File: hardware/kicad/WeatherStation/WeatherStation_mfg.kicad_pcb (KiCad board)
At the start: 4 copper layers, 100 x 80 mm, 120 parts, among them J1 USB-C, J10 SOIL_TEMP, J11 LEAF_WET, J12 PYRANOMETER, J13 PANEL_TEMP_F, J14 PANEL_TEMP_B, J15 POWER_PULSE, J16 RS485_Bus, J18 SMA_WiFi, J19 RJ45_Magjack, J2 SOLAR_IN, J20 NanoSIM, J21 SMA_LTE, J22 MicroSD, J3 BATTERY, J4 ANEMOMETER, J5 RAIN_GAUGE, J6 SMA_LoRa, J7 DEBUG_UART, J8 SOIL_MOIST_1, J9 SOIL_MOIST_2, SW1 BOOT, SW2 RESET, SW3 MODE_DIP, U10 STM32F407VGT6, U11 MAX3485ESA+, U12 ATWINC1500, U13 RN4870-I/RM, U14 W5500, U15 SIM7600E-H, U16 TPS7A2033, U2 TP4056, U3 AMS1117-3.3, U4 BME280, U5 AS5600, U6 SI1145, U7 BH1750FVI, U8 SX1276/RFM95W, Y1 8MHz, Y2 25MHz

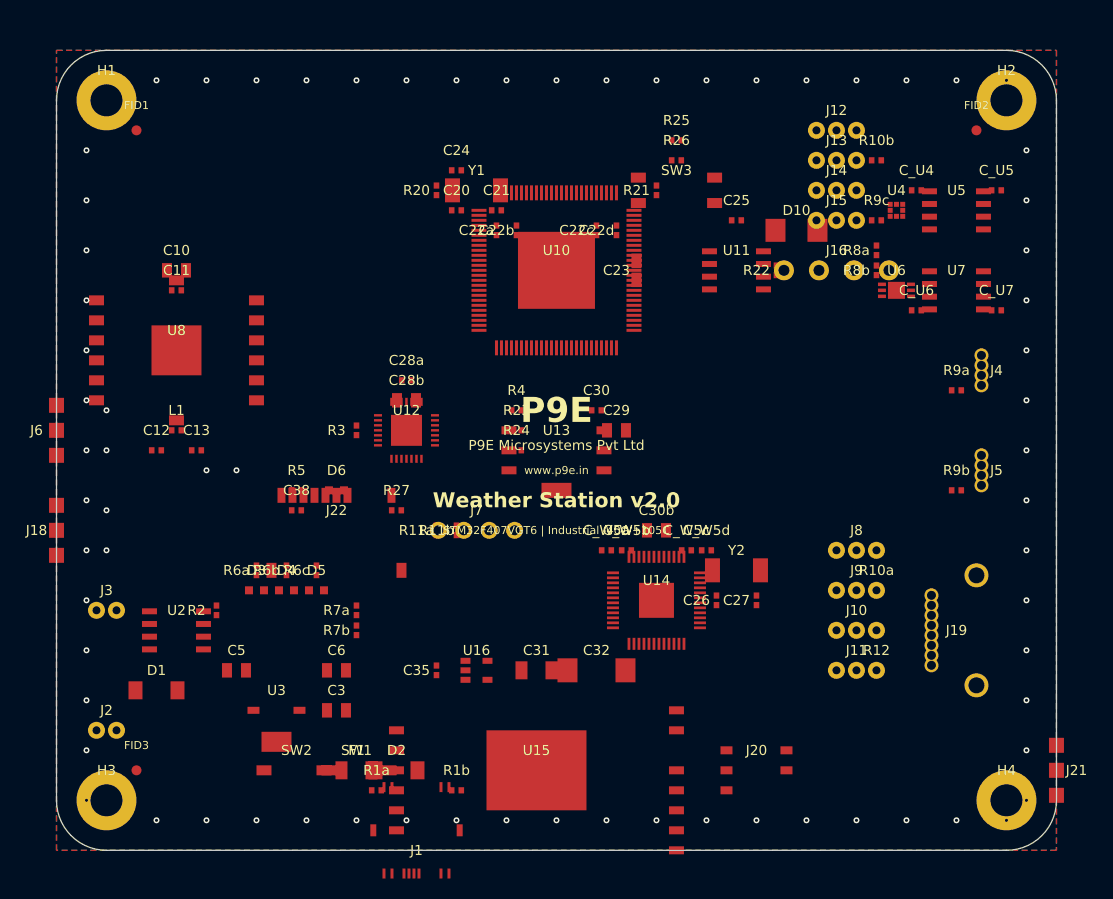
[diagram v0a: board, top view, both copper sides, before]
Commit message: fix: add 3 missing BOM components to manufacturing PCB
Add U2A (DW01A battery protection IC), Q1 (FS8205A dual N-MOSFET
for battery protection), and C4 (1uF AS5600 decoupling cap) that
were missing from the PCB layout. All BOM components now have
corresponding footprints in the manufacturing PCB.

https://claude.ai/code/session_01XHnfZQ5BbxTCTBMCteQyVe
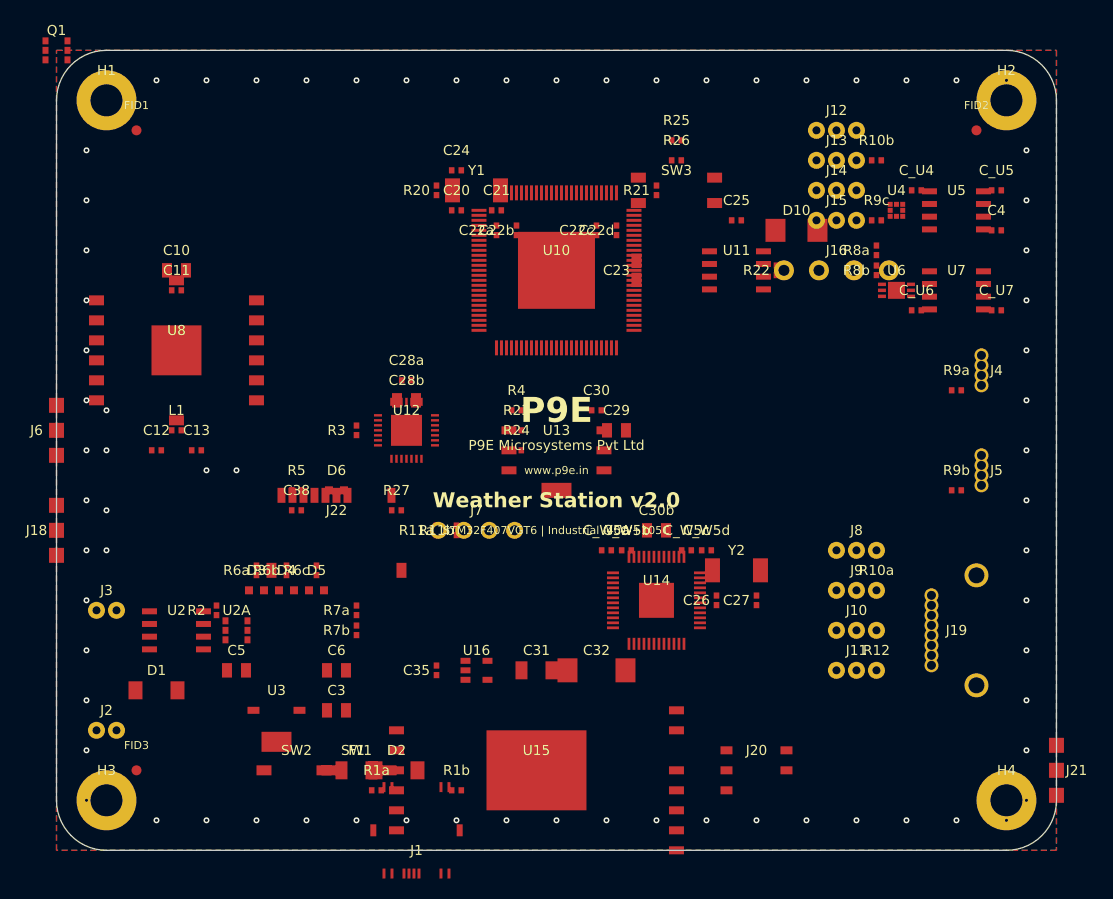
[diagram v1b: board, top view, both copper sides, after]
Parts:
- added C4: 1uF, Capacitor_SMD:C_0402_1005Metric, F.Cu at (94.0, 18.0)
- added Q1: FS8205A, Package_SO:SOT-23-6, F.Cu at (0.00, 58.0)
- added U2A: DW01A, Package_SO:SOT-23-6, F.Cu at (18.0, 58.0)
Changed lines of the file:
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@@
     (pad "2" smd rect (at 0.48 0) (size 0.56 0.62) (layers "F.Cu" "F.Paste" "F.Mask") (net 1 "GND"))
+  )
+  ;; U2A: DW01A Battery Protection IC (SOT-23-6) — paired with Q1
+  (footprint "Package_SO:SOT-23-6" (layer "F.Cu")
+    (tstamp "fp-u2a-0001")
+    (at 18 58)
+    (property "Reference" "U2A" (at 0 -2) (layer "F.SilkS") (effects (font (size 1 1) (thickness 0.15))))
+    (property "Value" "DW01A" (at 0 2) (layer "F.Fab") (effects (font (size 1 1) (thickness 0.15))))
+    (pad "1" smd rect (at -1.1 -0.95) (size 0.6 0.7) (layers "F.Cu" "F.Paste" "F.Mask") (net 0 ""))
+    (pad "2" smd rect (at -1.1 0) (size 0.6 0.7) (layers "F.Cu" "F.Paste" "F.Mask") (net 1 "GND"))
+    (pad "3" smd rect (at -1.1 0.95) (size 0.6 0.7) (layers "F.Cu" "F.Paste" "F.Mask") (net 0 ""))
+    (pad "4" smd rect (at 1.1 0.95) (size 0.6 0.7) (layers "F.Cu" "F.Paste" "F.Mask") (net 0 ""))
+    (pad "5" smd rect (at 1.1 0) (size 0.6 0.7) (layers "F.Cu" "F.Paste" "F.Mask") (net 4 "VBAT"))
+    (pad "6" smd rect (at 1.1 -0.95) (size 0.6 0.7) (layers "F.Cu" "F.Paste" "F.Mask") (net 4 "VBAT"))
+  )
+  ;; Q1: FS8205A Dual N-MOSFET for battery protection (SOT-23-6)
+  (footprint "Package_SO:SOT-23-6" (layer "F.Cu")
+    (tstamp "fp-q1-0001")
+    (at 22, 58)
+    (property "Reference" "Q1" (at 0 -2) (layer "F.SilkS") (effects (font (size 1 1) (thickness 0.15))))
+    (property "Value" "FS8205A" (at 0 2) (layer "F.Fab") (effects (font (size 1 1) (thickness 0.15))))
+    (pad "1" smd rect (at -1.1 -0.95) (size 0.6 0.7) (layers "F.Cu" "F.Paste" "F.Mask") (net 1 "GND"))
+    (pad "2" smd rect (at -1.1 0) (size 0.6 0.7) (layers "F.Cu" "F.Paste" "F.Mask") (net 1 "GND"))
+    (pad "3" smd rect (at -1.1 0.95) (size 0.6 0.7) (layers "F.Cu" "F.Paste" "F.Mask") (net 0 ""))
+    (pad "4" smd rect (at 1.1 0.95) (size 0.6 0.7) (layers "F.Cu" "F.Paste" "F.Mask") (net 0 ""))
+    (pad "5" smd rect (at 1.1 0) (size 0.6 0.7) (layers "F.Cu" "F.Paste" "F.Mask") (net 4 "VBAT"))
+    (pad "6" smd rect (at 1.1 -0.95) (size 0.6 0.7) (layers "F.Cu" "F.Paste" "F.Mask") (net 4 "VBAT"))
   )
   (footprint "Connector_JST:JST_PH_B2B-PH-K_1x02_P2.00mm_Vertical" (layer "F.Cu")
@@
     (pad "1" smd rect (at -0.48 0) (size 0.56 0.62) (layers "F.Cu" "F.Paste" "F.Mask") (net 2 "+3V3"))
     (pad "2" smd rect (at 0.48 0) (size 0.56 0.62) (layers "F.Cu" "F.Paste" "F.Mask") (net 1 "GND"))
+  )
+  ;; C4: 1uF AS5600 decoupling capacitor
+  (footprint "Capacitor_SMD:C_0402_1005Metric" (layer "F.Cu")
+    (tstamp "fp-c4-0001")
+    (at 94 18)
+    (property "Reference" "C4" (at 0 -2) (layer "F.SilkS") (effects (font (size 1 1) (thickness 0.15))))
+    (property "Value" "1uF" (at 0 2) (layer "F.Fab") (effects (font (size 1 1) (thickness 0.15))))
+    (pad "1" smd rect (at -0.48 0) (size 0.56 0.62) (layers "F.Cu" "F.Paste" "F.Mask") (net 2 "+3V3"))
+    (pad "2" smd rect (at 0.48 0) (size 0.56 0.62) (layers "F.Cu" "F.Paste" "F.Mask") (net 1 "GND"))

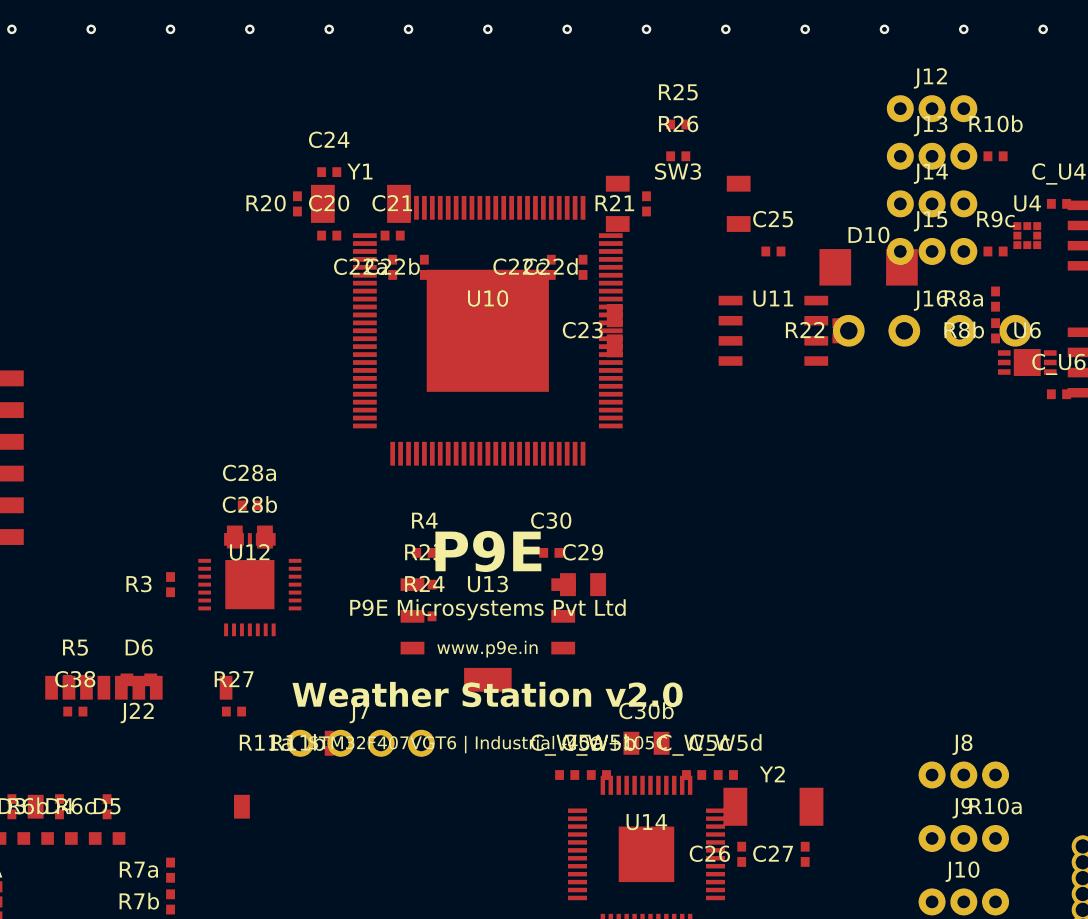
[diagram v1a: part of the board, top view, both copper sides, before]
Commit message: fix: correct connector pin counts, capacitor size, and add R6d
Fixes from detailed BOM cross-reference audit:

- J12 (Pyranometer): Changed from 3-pin to 4-pin JST (B4B-PH-K)
  per BOM spec (V+/GND/OUT/EN)
- J15 (Power Pulse): Changed from 3-pin to 2-pin JST (B2B-PH-K)
  per BOM spec (SIG/GND, S0 pulse interface)
- C30 (W5500 bulk decoupling): Fixed from 0402/100nF to 0805/10uF
  per BOM specification
- R6d: Added 4th 1k LED series resistor (BOM Qty=4, only 3 existed)

All 124 component references now match BOM specifications.

https://claude.ai/code/session_01XHnfZQ5BbxTCTBMCteQyVe
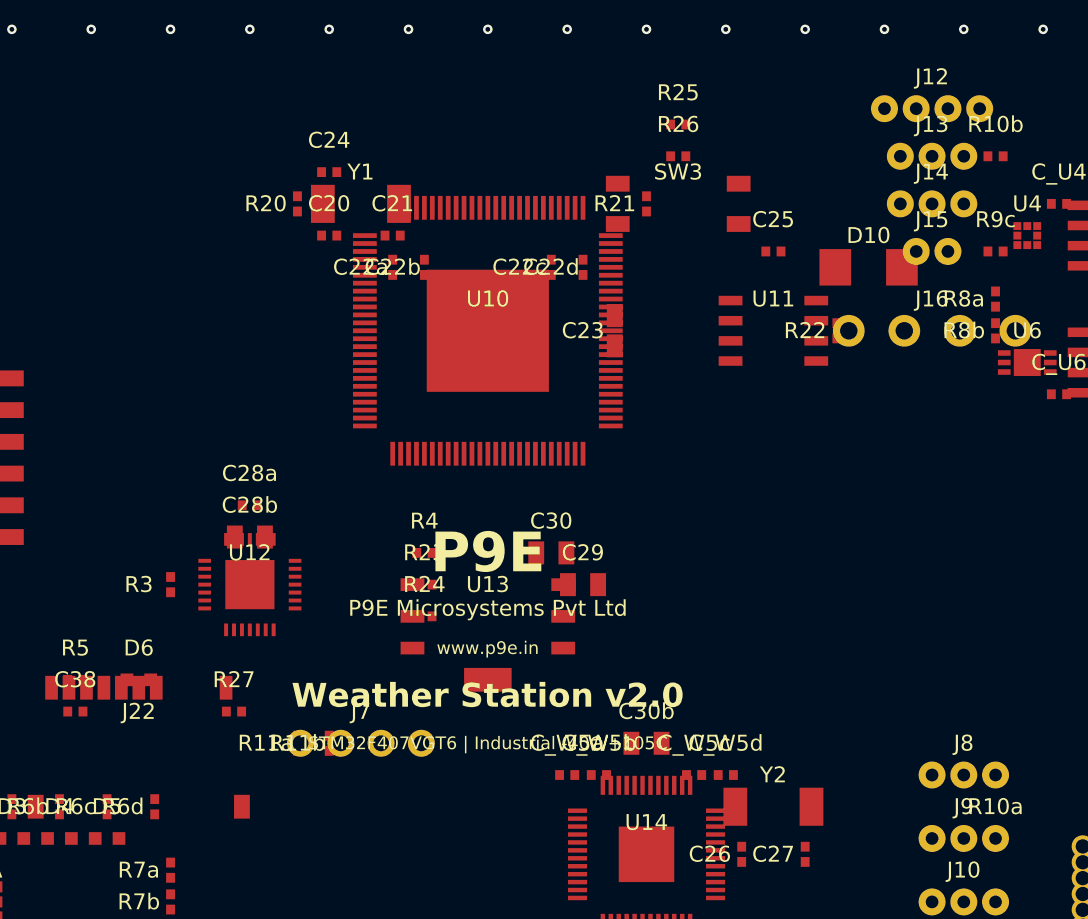
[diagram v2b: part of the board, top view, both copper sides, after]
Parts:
- added R6d: 1k, Resistor_SMD:R_0402_1005Metric, F.Cu at (29.0, 52.0)
- C30: value 100nF -> 10uF; footprint Capacitor_SMD:C_0402_1005Metric -> Capacitor_SMD:C_0805_2012Metric
- J12: footprint Connector_JST:JST_PH_B3B-PH-K_1x03_P2.00mm_Vertical -> Connector_JST:JST_PH_B4B-PH-K_1x04_P2.00mm_Vertical
- J15: footprint Connector_JST:JST_PH_B3B-PH-K_1x03_P2.00mm_Vertical -> Connector_JST:JST_PH_B2B-PH-K_1x02_P2.00mm_Vertical
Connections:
- J15 pad 1: +3V3 -> POWER_PULSE
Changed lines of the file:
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@@
+    (pad "2" smd rect (at 0.48 0) (size 0.56 0.62) (layers "F.Cu" "F.Paste" "F.Mask") (net 0 ""))
+  )
+  ;; R6d: 4th LED series resistor (spare, per BOM Qty=4)
+  (footprint "Resistor_SMD:R_0402_1005Metric" (layer "F.Cu")
+    (tstamp "fp-r6d-0001")
+    (at 29 52 90)
+    (property "Reference" "R6d" (at 0 -2) (layer "F.SilkS") (effects (font (size 1 1) (thickness 0.15))))
+    (property "Value" "1k" (at 0 2) (layer "F.Fab") (effects (font (size 1 1) (thickness 0.15))))
+    (pad "1" smd rect (at -0.48 0) (size 0.56 0.62) (layers "F.Cu" "F.Paste" "F.Mask") (net 0 ""))
     (pad "2" smd rect (at 0.48 0) (size 0.56 0.62) (layers "F.Cu" "F.Paste" "F.Mask") (net 0 ""))
   )
@@
     (pad "7" smd rect (at 0 4) (size 3.0 1.5) (layers "F.Cu" "F.Paste" "F.Mask") (net 1 "GND"))
   )
-  (footprint "Capacitor_SMD:C_0402_1005Metric" (layer "F.Cu")
+  (footprint "Capacitor_SMD:C_0805_2012Metric" (layer "F.Cu")
     (tstamp "fp-c30-0001")
     (at 54 36)
     (property "Reference" "C30" (at 0 -2) (layer "F.SilkS") (effects (font (size 1 1) (thickness 0.15))))
-    (property "Value" "100nF" (at 0 2) (layer "F.Fab") (effects (font (size 1 1) (thickness 0.15))))
-    (pad "1" smd rect (at -0.48 0) (size 0.56 0.62) (layers "F.Cu" "F.Paste" "F.Mask") (net 2 "+3V3"))
-    (pad "2" smd rect (at 0.48 0) (size 0.56 0.62) (layers "F.Cu" "F.Paste" "F.Mask") (net 1 "GND"))
+    (property "Value" "10uF" (at 0 2) (layer "F.Fab") (effects (font (size 1 1) (thickness 0.15))))
+    (pad "1" smd rect (at -0.95 0) (size 1.0 1.45) (layers "F.Cu" "F.Paste" "F.Mask") (net 2 "+3V3"))
+    (pad "2" smd rect (at 0.95 0) (size 1.0 1.45) (layers "F.Cu" "F.Paste" "F.Mask") (net 1 "GND"))
   )
   (footprint "Capacitor_SMD:C_0805_2012Metric" (layer "F.Cu")
@@
     (pad "3" thru_hole circle (at 2.0 0) (size 1.7 1.7) (drill 0.8) (layers "*.Cu" "*.Mask") (net 89 "LEAF_WET_SIG"))
   )
-  (footprint "Connector_JST:JST_PH_B3B-PH-K_1x03_P2.00mm_Vertical" (layer "F.Cu")
+  (footprint "Connector_JST:JST_PH_B4B-PH-K_1x04_P2.00mm_Vertical" (layer "F.Cu")
     (tstamp "fp-j12-0001")
     (at 78 8)
     (property "Reference" "J12" (at 0 -2) (layer "F.SilkS") (effects (font (size 1 1) (thickness 0.15))))
     (property "Value" "PYRANOMETER" (at 0 2) (layer "F.Fab") (effects (font (size 1 1) (thickness 0.15))))
-    (pad "1" thru_hole circle (at -2.0 0) (size 1.7 1.7) (drill 0.8) (layers "*.Cu" "*.Mask") (net 2 "+3V3"))
-    (pad "2" thru_hole circle (at 0 0) (size 1.7 1.7) (drill 0.8) (layers "*.Cu" "*.Mask") (net 1 "GND"))
-    (pad "3" thru_hole circle (at 2.0 0) (size 1.7 1.7) (drill 0.8) (layers "*.Cu" "*.Mask") (net 90 "PYRANO_OUT"))
+    (pad "1" thru_hole circle (at -3.0 0) (size 1.7 1.7) (drill 0.8) (layers "*.Cu" "*.Mask") (net 2 "+3V3"))
+    (pad "2" thru_hole circle (at -1.0 0) (size 1.7 1.7) (drill 0.8) (layers "*.Cu" "*.Mask") (net 1 "GND"))
+    (pad "3" thru_hole circle (at 1.0 0) (size 1.7 1.7) (drill 0.8) (layers "*.Cu" "*.Mask") (net 90 "PYRANO_OUT"))
+    (pad "4" thru_hole circle (at 3.0 0) (size 1.7 1.7) (drill 0.8) (layers "*.Cu" "*.Mask") (net 0 ""))
   )
   (footprint "Connector_JST:JST_PH_B3B-PH-K_1x03_P2.00mm_Vertical" (layer "F.Cu")
@@
     (pad "3" thru_hole circle (at 2.0 0) (size 1.7 1.7) (drill 0.8) (layers "*.Cu" "*.Mask") (net 92 "PANEL_TEMP2_DATA"))
   )
-  (footprint "Connector_JST:JST_PH_B3B-PH-K_1x03_P2.00mm_Vertical" (layer "F.Cu")
+  (footprint "Connector_JST:JST_PH_B2B-PH-K_1x02_P2.00mm_Vertical" (layer "F.Cu")
     (tstamp "fp-j15-0001")
     (at 78 17)
     (property "Reference" "J15" (at 0 -2) (layer "F.SilkS") (effects (font (size 1 1) (thickness 0.15))))
     (property "Value" "POWER_PULSE" (at 0 2) (layer "F.Fab") (effects (font (size 1 1) (thickness 0.15))))
-    (pad "1" thru_hole circle (at -2.0 0) (size 1.7 1.7) (drill 0.8) (layers "*.Cu" "*.Mask") (net 2 "+3V3"))
-    (pad "2" thru_hole circle (at 0 0) (size 1.7 1.7) (drill 0.8) (layers "*.Cu" "*.Mask") (net 1 "GND"))
-    (pad "3" thru_hole circle (at 2.0 0) (size 1.7 1.7) (drill 0.8) (layers "*.Cu" "*.Mask") (net 93 "POWER_PULSE"))
-  )
-  (footprint "Resistor_SMD:R_0402_1005Metric" (layer "F.Cu")
+    (pad "1" thru_hole circle (at -1.0 0) (size 1.7 1.7) (drill 0.8) (layers "*.Cu" "*.Mask") (net 93 "POWER_PULSE"))
+    (pad "2" thru_hole circle (at 1.0 0) (size 1.7 1.7) (drill 0.8) (layers "*.Cu" "*.Mask") (net 1 "GND"))
+  )
+  (footprint "Resistor_SMD:R_0402_1005Metric" (layer "F.Cu")
